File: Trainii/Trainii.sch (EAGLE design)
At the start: 42 parts, among them J1 APDS-9960, J2 Left Motor Encoder, J3 Right Motor Encoder, J4 Line Sensor 1, J5 Line Sensor 2, J6 Ultrasonic, J7 Left Motor Output, J8 Right Motor Output, J9 Lift Motor Output, T1 MCH3383SC-70FL, T2 MCH3383SC-70FL, T3 MCH3383SC-70FL, U1 TPS61222DCKR, U2 BSS138, X1 JST-PH2

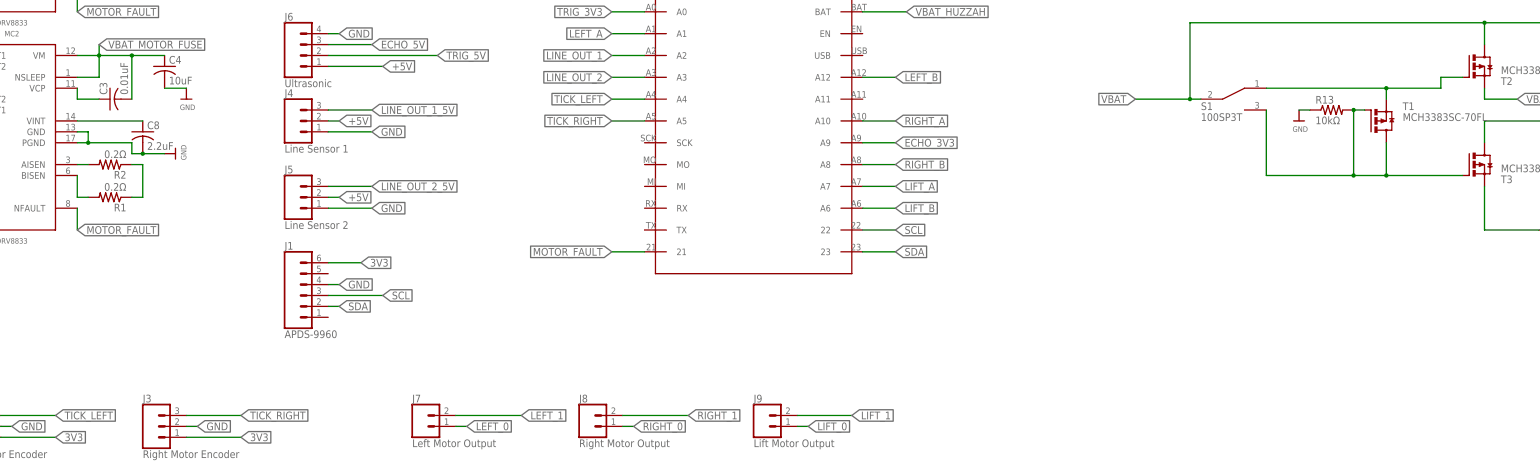
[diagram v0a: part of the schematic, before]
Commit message: Initial component placement before routing
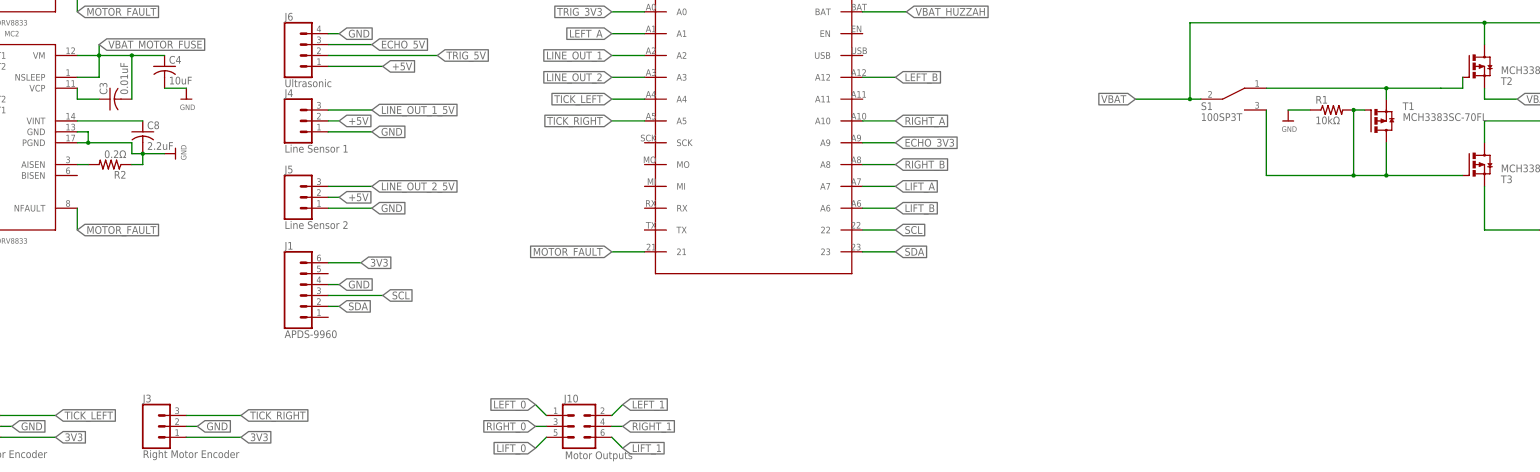
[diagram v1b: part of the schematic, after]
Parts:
- removed J7: Left Motor Output, SparkFun-Connectors:CONN_02
- removed J8: Right Motor Output, SparkFun-Connectors:CONN_02
- removed J9: Lift Motor Output, SparkFun-Connectors:CONN_02
- removed R13: 10kΩ, rcl:R-US_R0603
- added J10: Motor Outputs, SparkFun-Connectors:CONN_03X2FEMALE
- R1: value 0.2Ω -> 10kΩ; device rcl:R-US_R0805 -> rcl:R-US_R0603
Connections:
- removed net N$2: R1.1, R2.1
- removed net N$4: MC2.BISEN, R1.2
- net GND: now also R1.1, R2.1; no longer R13.1
- net LEFT_0: now also J10.1; no longer J7.1
- net LEFT_1: now also J10.2; no longer J7.2
- net LIFT_0: now also J10.5; no longer J9.1
- net LIFT_1: now also J10.6; no longer J9.2
- net N$13: now also R1.2; no longer R13.2
- net RIGHT_0: now also J10.3; no longer J8.1
- net RIGHT_1: now also J10.4; no longer J8.2
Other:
- moved on the sheet: R1
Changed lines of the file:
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@@
 <part name="J5" library="SparkFun-Connectors" library_urn="urn:adsk.eagle:library:513" deviceset="CONN_03" device="" package3d_urn="urn:adsk.eagle:package:38063/1" value="Line Sensor 2"/>
 <part name="J6" library="SparkFun-Connectors" library_urn="urn:adsk.eagle:library:513" deviceset="CONN_04" device="" package3d_urn="urn:adsk.eagle:package:38085/1" value="Ultrasonic"/>
-<part name="J7" library="SparkFun-Connectors" library_urn="urn:adsk.eagle:library:513" deviceset="CONN_02" device="" package3d_urn="urn:adsk.eagle:package:38039/1" value="Left Motor Output"/>
-<part name="J8" library="SparkFun-Connectors" library_urn="urn:adsk.eagle:library:513" deviceset="CONN_02" device="" package3d_urn="urn:adsk.eagle:package:38039/1" value="Right Motor Output"/>
-<part name="J9" library="SparkFun-Connectors" library_urn="urn:adsk.eagle:library:513" deviceset="CONN_02" device="" package3d_urn="urn:adsk.eagle:package:38039/1" value="Lift Motor Output"/>
 <part name="MC2" library="Trainii" deviceset="DRV8833" device=""/>
 <part name="C3" library="rcl" library_urn="urn:adsk.eagle:library:334" deviceset="C-US" device="C0805" package3d_urn="urn:adsk.eagle:package:23617/2" value="0.01uF"/>
 <part name="U$4" library="microbuilder" deviceset="GND" device=""/>
 <part name="C4" library="rcl" library_urn="urn:adsk.eagle:library:334" deviceset="C-US" device="C0805" package3d_urn="urn:adsk.eagle:package:23617/2" value="10uF"/>
-<part name="R1" library="rcl" library_urn="urn:adsk.eagle:library:334" deviceset="R-US_" device="R0805" package3d_urn="urn:adsk.eagle:package:23553/2" value="0.2Ω"/>
 <part name="R2" library="rcl" library_urn="urn:adsk.eagle:library:334" deviceset="R-US_" device="R0805" package3d_urn="urn:adsk.eagle:package:23553/2" value="0.2Ω"/>
 <part name="MC1" library="Trainii" deviceset="DRV8833" device=""/>
@@
 <part name="T3" library="Trainii" deviceset="MCH3383" device="SC-70FL" package3d_urn="urn:adsk.eagle:package:4252167/1"/>
 <part name="T1" library="Trainii" deviceset="MCH3383" device="SC-70FL" package3d_urn="urn:adsk.eagle:package:4252167/1"/>
-<part name="R13" library="rcl" library_urn="urn:adsk.eagle:library:334" deviceset="R-US_" device="R0603" package3d_urn="urn:adsk.eagle:package:23555/2" value="10kΩ"/>
+<part name="R1" library="rcl" library_urn="urn:adsk.eagle:library:334" deviceset="R-US_" device="R0603" package3d_urn="urn:adsk.eagle:package:23555/2" value="10kΩ"/>
 <part name="U$19" library="microbuilder" deviceset="GND" device=""/>
 <part name="U$20" library="microbuilder" deviceset="GND" device=""/>
+<part name="J10" library="SparkFun-Connectors" library_urn="urn:adsk.eagle:library:513" deviceset="CONN_03X2" device="FEMALE" package3d_urn="urn:adsk.eagle:package:38016/1" value="Motor Outputs"/>
 </parts>
 <sheets>
@@
 <instance part="J5" gate="J$1" x="101.6" y="160.02"/>
 <instance part="J6" gate="G$1" x="104.14" y="193.04"/>
-<instance part="J7" gate="G$1" x="131.318" y="106.68"/>
-<instance part="J8" gate="G$1" x="170.18" y="106.68"/>
-<instance part="J9" gate="G$1" x="210.82" y="106.68"/>
 <instance part="MC2" gate="G$1" x="35.56" y="175.26"/>
 <instance part="C3" gate="G$1" x="58.42" y="182.88" rot="R90"/>
 <instance part="U$4" gate="G$1" x="73.66" y="170.18" rot="R90"/>
 <instance part="C4" gate="G$1" x="71.12" y="190.5"/>
-<instance part="R1" gate="G$1" x="58.42" y="160.02" rot="R180"/>
 <instance part="R2" gate="G$1" x="58.42" y="167.64" rot="R180"/>
 <instance part="MC1" gate="G$1" x="35.56" y="226.06"/>
@@
 <instance part="T3" gate="G$1" x="375.92" y="167.64" rot="MR180"/>
 <instance part="T1" gate="G$1" x="353.06" y="177.8"/>
-<instance part="R13" gate="G$1" x="342.9" y="180.34"/>
+<instance part="R1" gate="G$1" x="342.9" y="180.34"/>
 <instance part="U$19" gate="G$1" x="254" y="241.3"/>
-<instance part="U$20" gate="G$1" x="335.28" y="177.8"/>
+<instance part="U$20" gate="G$1" x="332.74" y="177.8"/>
+<instance part="J10" gate="G$1" x="167.64" y="106.68"/>
 </instances>
 <busses>
@@
 <wire x1="66.04" y1="170.18" x2="71.12" y2="170.18" width="0.1524" layer="91"/>
 <junction x="66.04" y="170.18"/>
+<pinref part="R2" gate="G$1" pin="1"/>
+<wire x1="63.5" y1="167.64" x2="66.04" y2="167.64" width="0.1524" layer="91"/>
+<wire x1="66.04" y1="167.64" x2="66.04" y2="170.18" width="0.1524" layer="91"/>
 </segment>
 <segment>
@@
 </segment>
 <segment>
-<pinref part="R13" gate="G$1" pin="1"/>
+<pinref part="R1" gate="G$1" pin="1"/>
 <pinref part="U$20" gate="G$1" pin="GND"/>
-<wire x1="335.28" y1="180.34" x2="337.82" y2="180.34" width="0.1524" layer="91"/>
+<wire x1="332.74" y1="180.34" x2="337.82" y2="180.34" width="0.1524" layer="91"/>
 </segment>
 <segment>
@@
 </segment>
 </net>
-<net name="N$4" class="0">
-<segment>
-<pinref part="R1" gate="G$1" pin="2"/>
-<pinref part="MC2" gate="G$1" pin="BISEN"/>
-<wire x1="53.34" y1="160.02" x2="50.8" y2="160.02" width="0.1524" layer="91"/>
-<wire x1="50.8" y1="160.02" x2="50.8" y2="165.1" width="0.1524" layer="91"/>
-</segment>
-</net>
 <net name="N$6" class="0">
 <segment>
@@
 </segment>
 <segment>
-<pinref part="J7" gate="G$1" pin="1"/>
-<wire x1="138.938" y1="106.68" x2="141.478" y2="106.68" width="0.1524" layer="91"/>
-<label x="141.478" y="106.68" size="1.778" layer="95" xref="yes"/>
+<pinref part="J10" gate="G$1" pin="1"/>
+<wire x1="160.02" y1="109.22" x2="157.48" y2="111.76" width="0.1524" layer="91"/>
+<label x="157.48" y="111.76" size="1.778" layer="95" rot="R180" xref="yes"/>
 </segment>
 </net>
 <net name="RIGHT_1" class="0">
-<segment>
-<pinref part="J8" gate="G$1" pin="2"/>
-<wire x1="177.8" y1="109.22" x2="193.04" y2="109.22" width="0.1524" layer="91"/>
-<label x="193.04" y="109.22" size="1.778" layer="95" xref="yes"/>
-</segment>
 <segment>
 <pinref part="MC1" gate="G$1" pin="BOUT2"/>
@@
 <label x="17.78" y="233.68" size="1.778" layer="95" rot="R180" xref="yes"/>
 </segment>
+<segment>
+<pinref part="J10" gate="G$1" pin="4"/>
+<wire x1="175.26" y1="106.68" x2="177.8" y2="106.68" width="0.1524" layer="91"/>
+<label x="177.8" y="106.68" size="1.778" layer="95" xref="yes"/>
+</segment>
 </net>
 <net name="LIFT_0" class="0">
-<segment>
-<pinref part="J9" gate="G$1" pin="1"/>
-<wire x1="218.44" y1="106.68" x2="220.98" y2="106.68" width="0.1524" layer="91"/>
-<label x="220.98" y="106.68" size="1.778" layer="95" xref="yes"/>
-</segment>
 <segment>
 <pinref part="MC2" gate="G$1" pin="AOUT1"/>
 <wire x1="20.32" y1="193.04" x2="17.78" y2="193.04" width="0.1524" layer="91"/>
 <label x="17.78" y="193.04" size="1.778" layer="95" rot="R180" xref="yes"/>
+</segment>
+<segment>
+<pinref part="J10" gate="G$1" pin="5"/>
+<wire x1="160.02" y1="104.14" x2="157.48" y2="101.6" width="0.1524" layer="91"/>
+<label x="157.48" y="101.6" size="1.778" layer="95" rot="R180" xref="yes"/>
 </segment>
 </net>
@@
 </segment>
 <segment>
-<pinref part="J9" gate="G$1" pin="2"/>
-<wire x1="218.44" y1="109.22" x2="231.14" y2="109.22" width="0.1524" layer="91"/>
-<label x="231.14" y="109.22" size="1.778" layer="95" xref="yes"/>
+<pinref part="J10" gate="G$1" pin="6"/>
+<wire x1="175.26" y1="104.14" x2="177.8" y2="101.6" width="0.1524" layer="91"/>
+<label x="177.8" y="101.6" size="1.778" layer="95" xref="yes"/>
 </segment>
 </net>
@@
 </segment>
 <segment>
-<pinref part="J8" gate="G$1" pin="1"/>
-<wire x1="177.8" y1="106.68" x2="180.34" y2="106.68" width="0.1524" layer="91"/>
-<label x="180.34" y="106.68" size="1.778" layer="95" xref="yes"/>
+<pinref part="J10" gate="G$1" pin="3"/>
+<wire x1="160.02" y1="106.68" x2="157.48" y2="106.68" width="0.1524" layer="91"/>
+<label x="157.48" y="106.68" size="1.778" layer="95" rot="R180" xref="yes"/>
 </segment>
 </net>
@@
 </segment>
 <segment>
-<pinref part="J7" gate="G$1" pin="2"/>
-<wire x1="138.938" y1="109.22" x2="154.178" y2="109.22" width="0.1524" layer="91"/>
-<label x="154.178" y="109.22" size="1.778" layer="95" xref="yes"/>
+<pinref part="J10" gate="G$1" pin="2"/>
+<wire x1="175.26" y1="109.22" x2="177.8" y2="111.76" width="0.1524" layer="91"/>
+<label x="177.8" y="111.76" size="1.778" layer="95" xref="yes"/>
 </segment>
 </net>
@@
 </segment>
 </net>
-<net name="N$2" class="0">
-<segment>
-<pinref part="R1" gate="G$1" pin="1"/>
-<pinref part="R2" gate="G$1" pin="1"/>
-<wire x1="63.5" y1="167.64" x2="66.04" y2="167.64" width="0.1524" layer="91"/>
-<wire x1="66.04" y1="167.64" x2="66.04" y2="160.02" width="0.1524" layer="91"/>
-<wire x1="66.04" y1="160.02" x2="63.5" y2="160.02" width="0.1524" layer="91"/>
-</segment>
-</net>
 <net name="N$5" class="0">
 <segment>
@@
 <segment>
 <pinref part="T2" gate="G$1" pin="G"/>
-<wire x1="373.38" y1="187.96" x2="368.3" y2="187.96" width="0.1524" layer="91"/>
+<wire x1="373.38" y1="187.96" x2="373.38" y2="185.42" width="0.1524" layer="91"/>
 <pinref part="S1" gate="G$1" pin="A"/>
-<wire x1="368.3" y1="187.96" x2="368.3" y2="185.42" width="0.1524" layer="91"/>
+<wire x1="373.38" y1="185.42" x2="368.3" y2="185.42" width="0.1524" layer="91"/>
 <wire x1="368.3" y1="185.42" x2="355.6" y2="185.42" width="0.1524" layer="91"/>
 <pinref part="T1" gate="G$1" pin="S"/>
@@
 <net name="N$13" class="0">
 <segment>
-<pinref part="R13" gate="G$1" pin="2"/>
+<pinref part="R1" gate="G$1" pin="2"/>
 <pinref part="T1" gate="G$1" pin="G"/>
 <wire x1="350.52" y1="180.34" x2="347.98" y2="180.34" width="0.1524" layer="91"/>

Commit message: Finished routing, exported images
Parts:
- removed J10: Motor Outputs, SparkFun-Connectors:CONN_03X2FEMALE
- added J7: Left Motor, SparkFun-Connectors:CONN_02
- added J8: Right Motor, SparkFun-Connectors:CONN_02
- added J9: Lift Motor, SparkFun-Connectors:CONN_02
- C5: value 10uF 6.3V -> 10uF 16V
- J2: value Left Motor Encoder -> Left Mtr Encoder
- J3: value Right Motor Encoder -> Right Mtr Encoder
- R1: device rcl:R-US_R0603 -> rcl:R-US_R0805
- renumbered U$6 to M1
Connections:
- removed net LINE_OUT_1: M1.A2
- removed net LINE_OUT_2: M1.A3
- net LEFT_0: now also J7.1; no longer J10.1
- net LEFT_1: now also J7.2; no longer J10.2
- net LIFT_0: now also J9.1; no longer J10.5
- net LIFT_1: now also J9.2; no longer J10.6
- net LINE_OUT_1_3V3: now also M1.A2
- net LINE_OUT_2_3V3: now also M1.A3
- net RIGHT_0: now also J8.1; no longer J10.3
- net RIGHT_1: now also J8.2; no longer J10.4

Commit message: Design Review Changes
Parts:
- removed R10, R12, R8: 91Ω, rcl:R-US_M0805
- removed R11, R7, R9: 47Ω, rcl:R-US_M0805
- R2, R3, R4: value 0.2Ω -> 10kΩ
- R5: value 10kΩ -> 47Ω; device rcl:R-US_R0805 -> rcl:R-US_M0805
- R6: value 10kΩ -> 91Ω; device rcl:R-US_R0805 -> rcl:R-US_M0805
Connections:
- removed net LINE_OUT_1_3V3: M1.A2, R10.1, R9.2
- removed net LINE_OUT_1_5V: J4.3, R9.1
- removed net LINE_OUT_2_3V3: M1.A3, R11.2, R12.1
- removed net LINE_OUT_2_5V: J5.3, R11.1
- removed net N$10: MC1.AISEN, R4.1
- removed net N$6: MC2.AISEN, R2.2
- removed net N$9: MC1.BISEN, R3.1
- new net LINE_OUT_1: J4.3, M1.A2
- new net LINE_OUT_2: J5.3, M1.A3
- net +5V: now also R4.1; no longer J4.2, J5.2, R6.1
- net 3V3: now also J4.2, J5.2, R2.2, R3.1; no longer R5.1
- net ECHO_3V3: now also M1.MI, R5.2, R6.1; no longer M1.A9, R7.2, R8.1
- net ECHO_5V: now also R5.1; no longer R7.1
- net GND: now also MC1.AISEN, MC1.BISEN, MC2.AISEN, MC2.BISEN, R6.2; no longer R10.2, R12.2, R2.1, R3.2, R4.2, R8.2
- net LEFT_B: now also M1.A10; no longer M1.A12
- net MOTOR_FAULT: now also R2.1
- net RIGHT_A: now also M1.A9; no longer M1.A10
- net TRIG_3V3: now also M1.MO, R3.2; no longer M1.A0, R5.2
- net TRIG_5V: now also R4.2; no longer R6.2
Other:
- moved on the sheet: R2, R3, R4, R5, R6

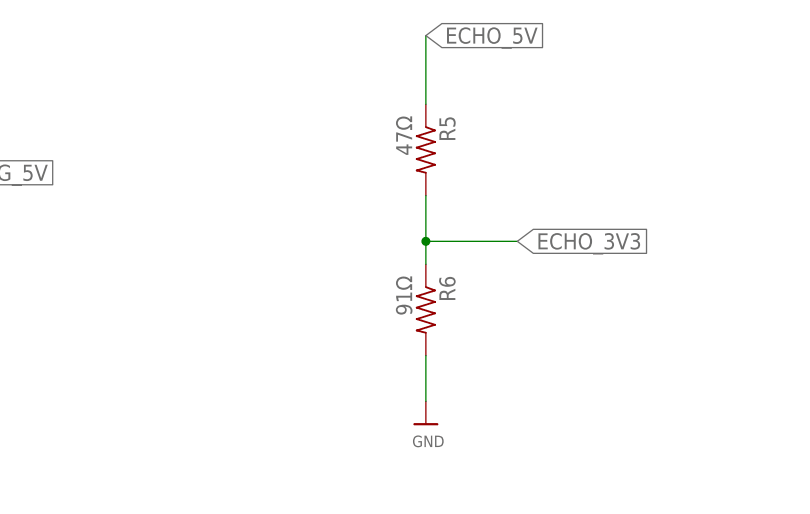
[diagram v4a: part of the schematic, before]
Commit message: Increase resistance to reduce current
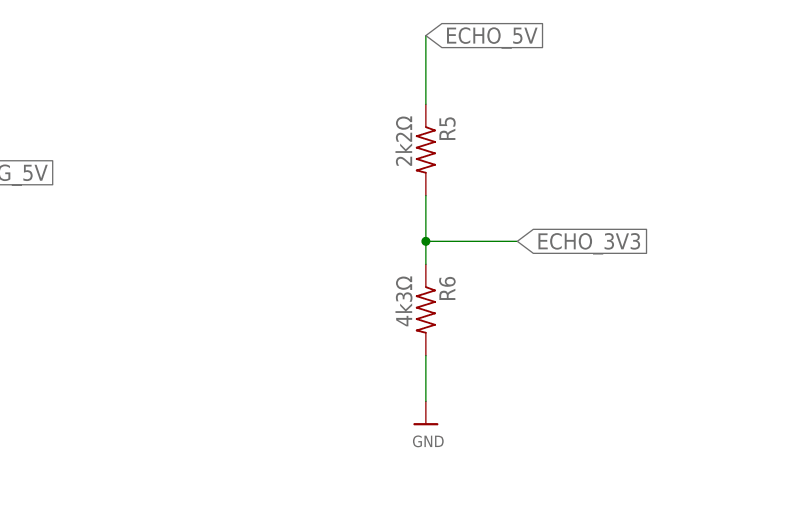
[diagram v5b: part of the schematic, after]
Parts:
- R5: value 47Ω -> 2k2Ω
- R6: value 91Ω -> 4k3Ω
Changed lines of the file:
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@@
 <part name="R4" library="rcl" library_urn="urn:adsk.eagle:library:334" deviceset="R-US_" device="R0805" package3d_urn="urn:adsk.eagle:package:23553/2" value="10kΩ"/>
 <part name="U2" library="Trainii" deviceset="BSS138" device=""/>
-<part name="R5" library="rcl" library_urn="urn:adsk.eagle:library:334" deviceset="R-US_" device="M0805" package3d_urn="urn:adsk.eagle:package:23556/1" value="47Ω"/>
-<part name="R6" library="rcl" library_urn="urn:adsk.eagle:library:334" deviceset="R-US_" device="M0805" package3d_urn="urn:adsk.eagle:package:23556/1" value="91Ω"/>
+<part name="R5" library="rcl" library_urn="urn:adsk.eagle:library:334" deviceset="R-US_" device="M0805" package3d_urn="urn:adsk.eagle:package:23556/1" value="2k2Ω"/>
+<part name="R6" library="rcl" library_urn="urn:adsk.eagle:library:334" deviceset="R-US_" device="M0805" package3d_urn="urn:adsk.eagle:package:23556/1" value="4k3Ω"/>
 <part name="U$13" library="microbuilder" deviceset="GND" device=""/>
 <part name="U1" library="Trainii" deviceset="TPS61222DCKR" device=""/>
